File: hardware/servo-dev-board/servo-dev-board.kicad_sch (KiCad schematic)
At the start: 39 parts, among them J1 USB_B_Micro, J2 Conn_01x05_MountingPin, J3 Conn_01x04_MountingPin, J4 Conn_01x04_MountingPin, J5 Conn_02x05_Odd_Even, SW1 SW_Push, SW2 SW_Push, U1 DRV8231ADSGR, U2 SSP7615-33DFR, U3 STM32F301K8Ux, Y1 16MHz 9pF

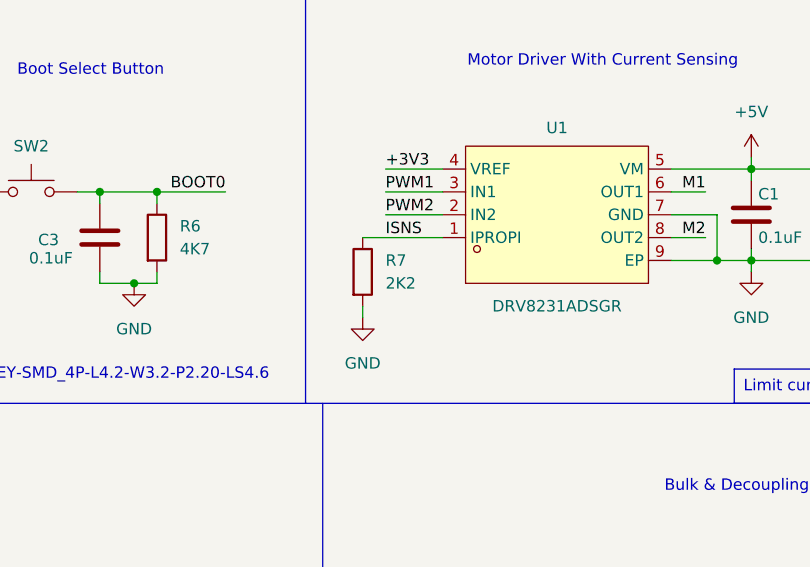
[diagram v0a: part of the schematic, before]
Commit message: Fixed error in PCB. Lowered isense resistor to 1.5k Ohm to increase max servo current to 1.5A
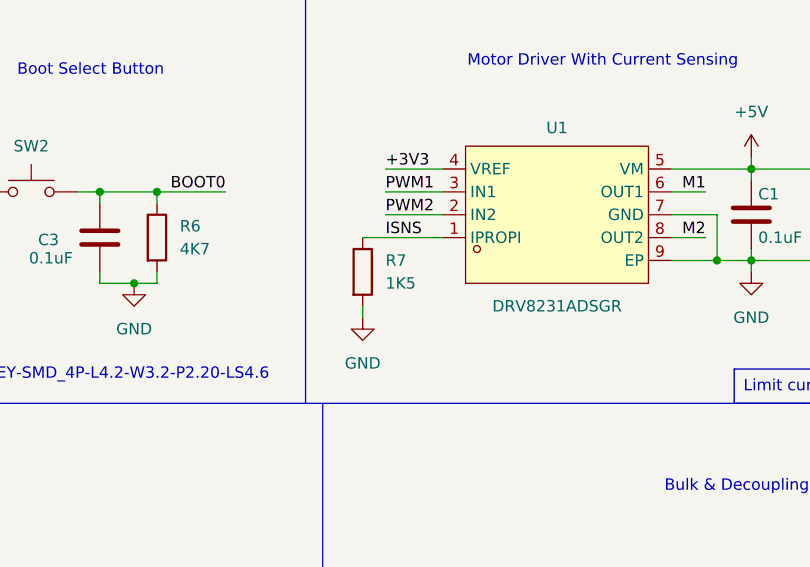
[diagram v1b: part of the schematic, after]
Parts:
- R7: value 2K2 -> 1K5; LCSC C25768 -> C25867
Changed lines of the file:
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@@
 			)
 		)
-		(property "Value" "2K2"
+		(property "Value" "1K5"
 			(at 110.49 88.8999 0)
 			(effects
@@
 			)
 		)
-		(property "LCSC" "C25768"
+		(property "LCSC" "C25867"
 			(at 110.49 86.3599 0)
 			(effects

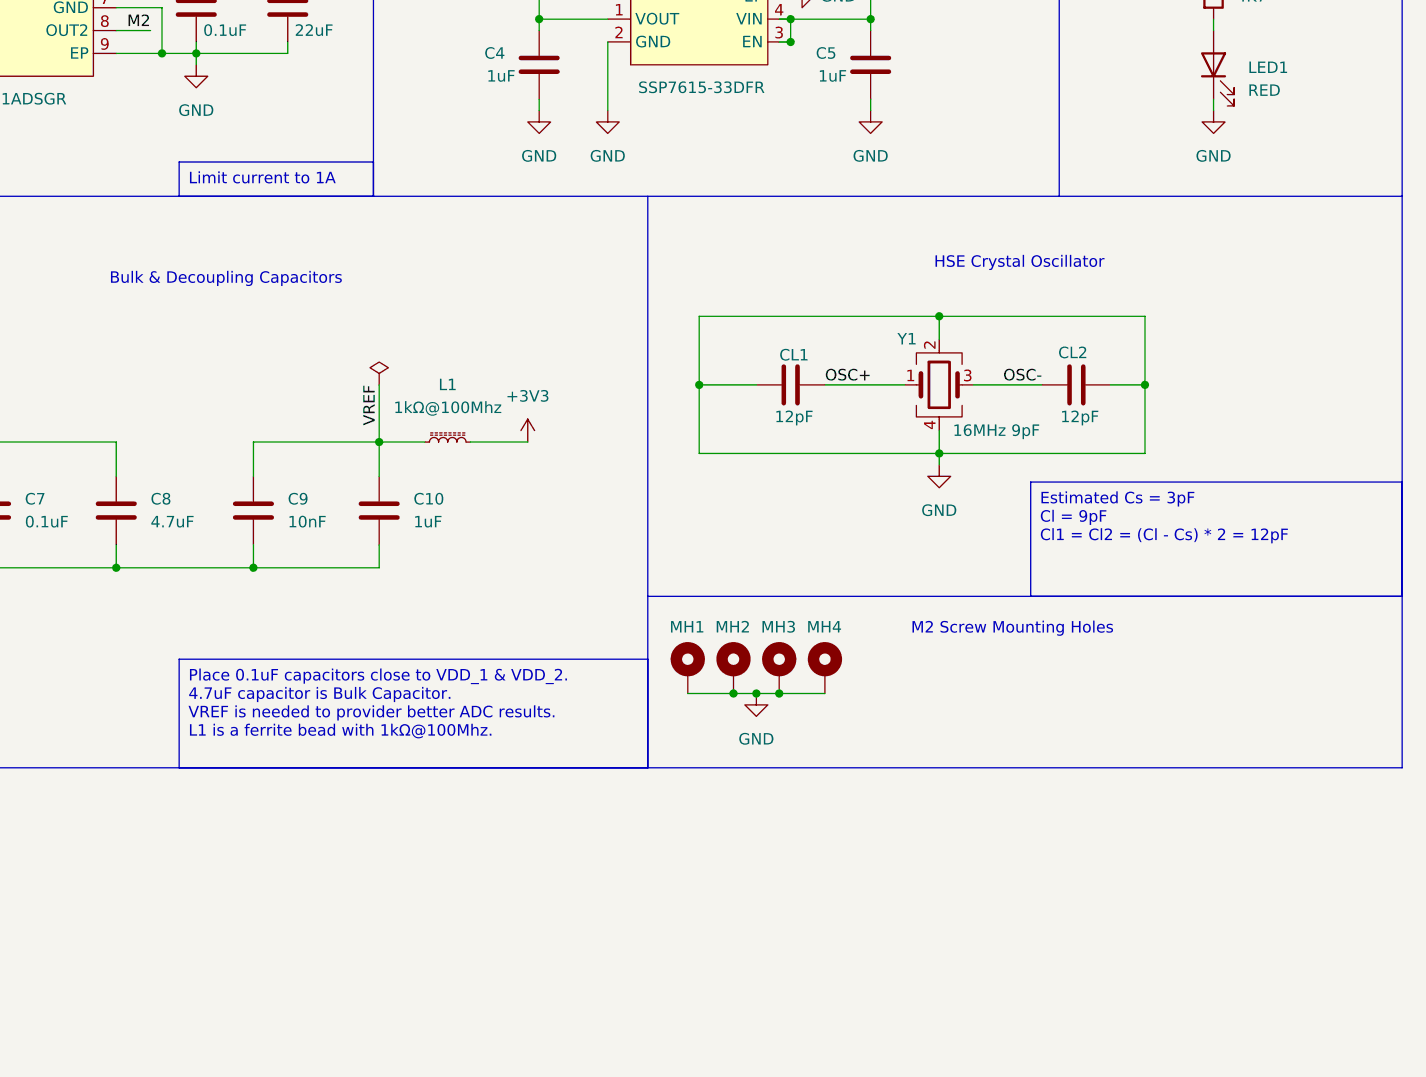
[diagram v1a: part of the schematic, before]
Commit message: added version, board, author info
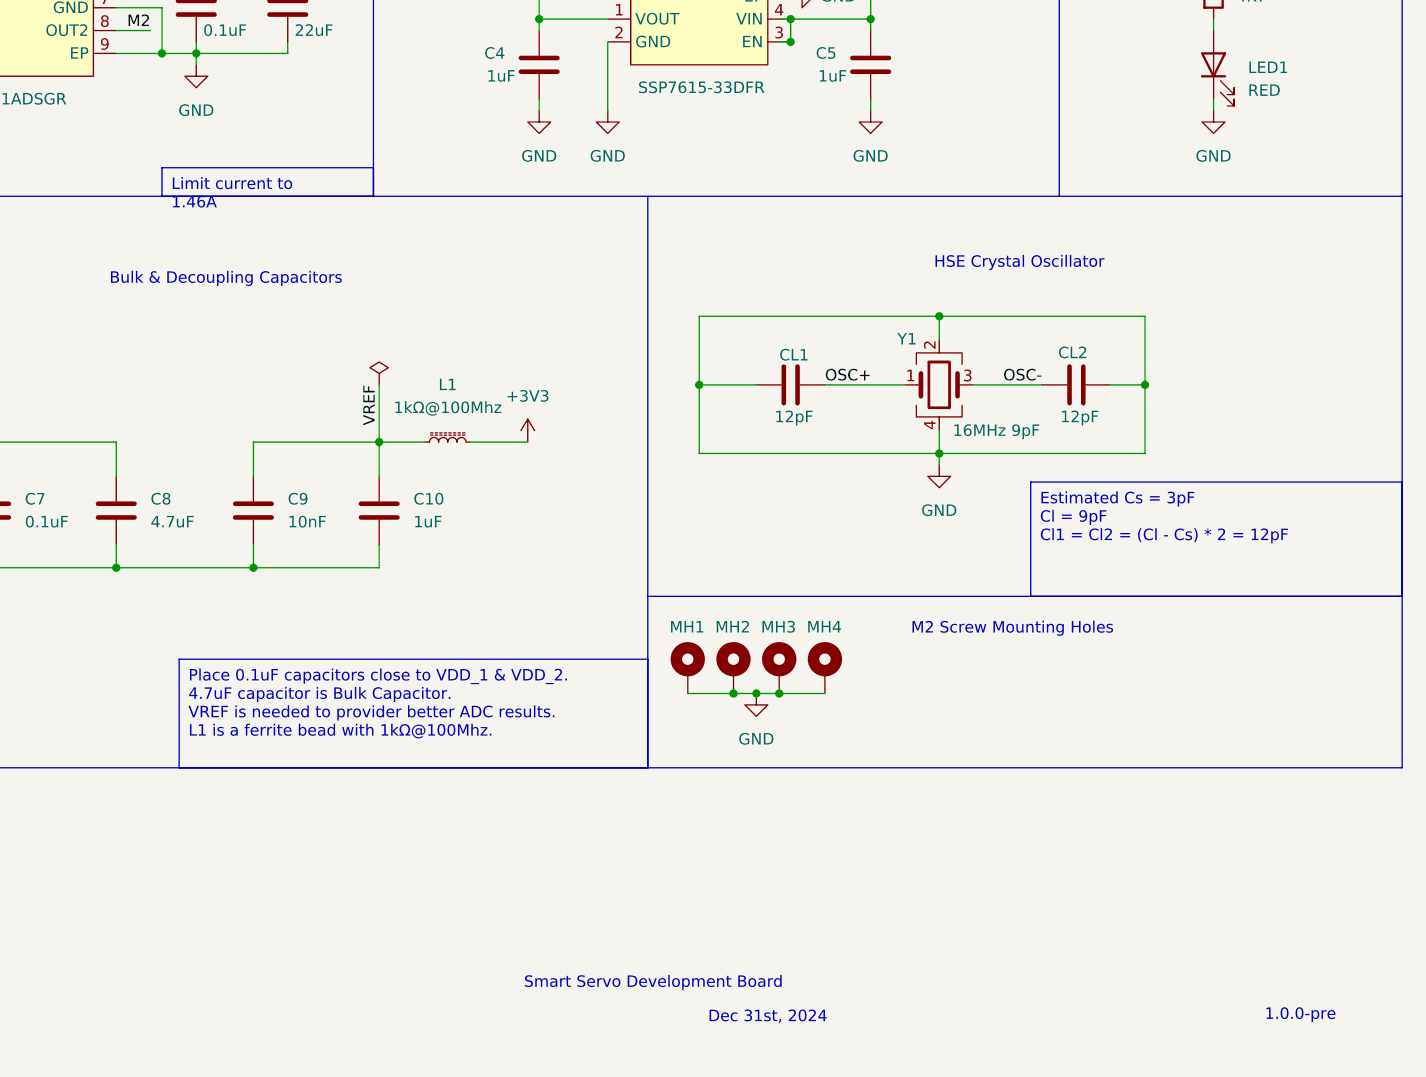
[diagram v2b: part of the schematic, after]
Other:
- note added: "1.0.0-pre"
- note added: "Dec 31st, 2024"
- note added: "Smart Servo Development Board"
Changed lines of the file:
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@@
 		)
 	)
-	(text_box "Limit current to 1A"
+	(text_box "Limit current to 1.46A"
 		(exclude_from_sim no)
-		(at 149.225 98.425 0)
-		(size 21.59 3.81)
+		(at 147.32 99.06 0)
+		(size 23.495 3.175)
 		(stroke
 			(width 0)
@@
 		)
 	)
+	(text "Dec 31st, 2024"
+		(exclude_from_sim no)
+		(at 214.63 193.548 0)
+		(effects
+			(font
+				(size 1.27 1.27)
+			)
+		)
+	)
 	(text "Reset Button"
 		(exclude_from_sim no)
 		(at 31.496 65.024 0)
+		(effects
+			(font
+				(size 1.27 1.27)
+			)
+		)
+	)
+	(text "Smart Servo Development Board"
+		(exclude_from_sim no)
+		(at 201.93 189.738 0)
 		(effects
 			(font
@@
 		(effects
 			(font
+				(size 1.27 1.27)
+			)
+		)
+	)
+	(text "1.0.0-pre"
+		(exclude_from_sim no)
+		(at 273.812 193.294 0)
+		(effects
+			(font

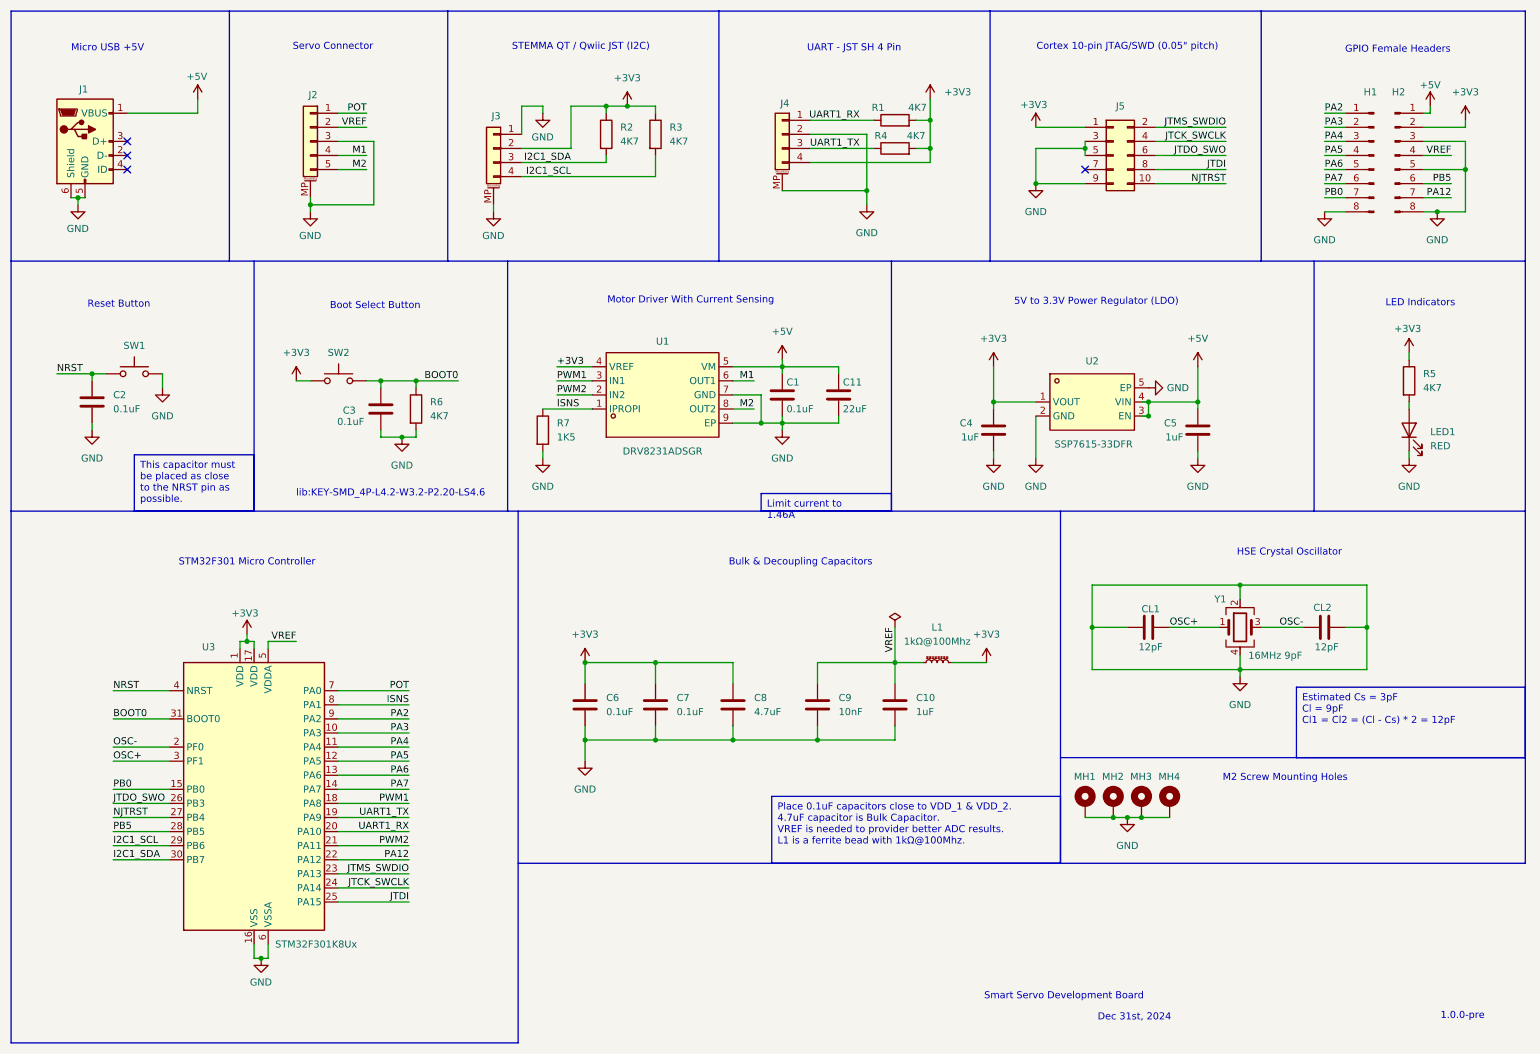
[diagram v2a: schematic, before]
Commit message: overhaul servo dev board to use ch32v00X
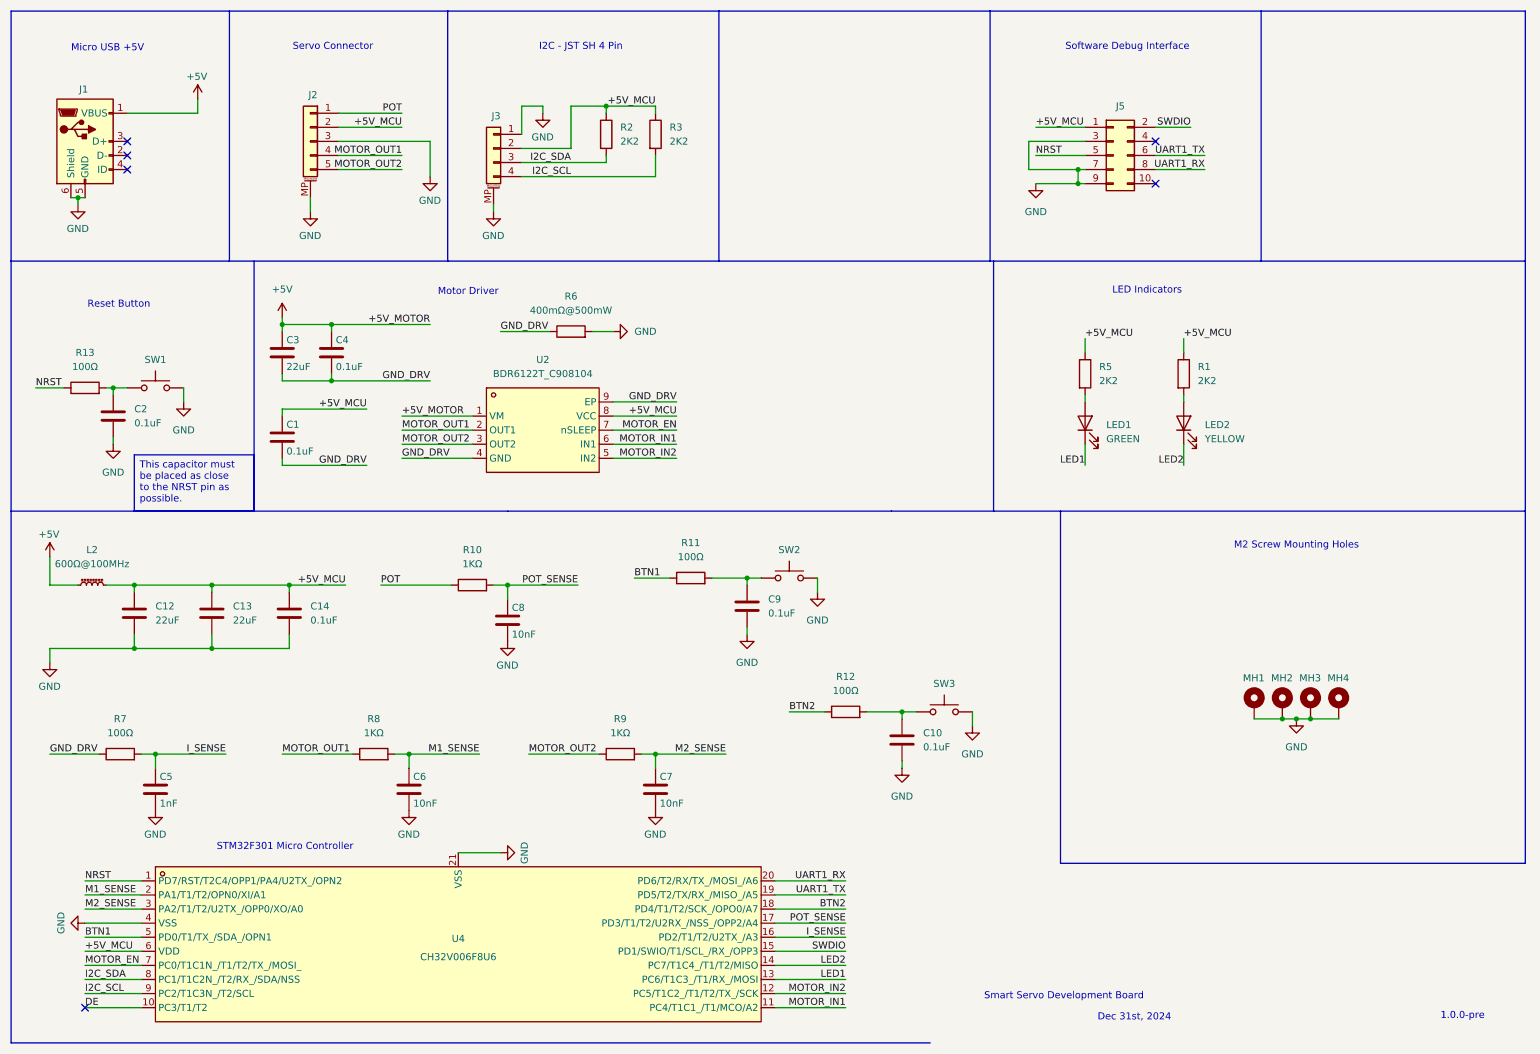
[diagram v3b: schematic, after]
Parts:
- removed C11: 22uF, Capacitor_SMD:C_0603_1608Metric, symbol Device:C
- removed CL1, CL2: 12pF, Capacitor_SMD:C_0402_1005Metric, symbol Device:C
- removed H1, H2: Conn_01x08_Pin, Connector_PinHeader_2.54mm:PinHeader_1x08_P2.54mm_Vertical, symbol Connector:Conn_01x08_Pin
- removed J4: Conn_01x04_MountingPin, Connector_JST:JST_SH_BM04B-SRSS-TB_1x04-1MP_P1.00mm_Vertical, symbol Connector_Generic_MountingPin:Conn_01x04_MountingPin
- removed L1: 1kΩ@100Mhz, Inductor_SMD:L_0402_1005Metric, symbol Device:L_Ferrite_Small
- removed R4: 4K7, Resistor_SMD:R_0402_1005Metric, symbol Device:R
- removed U1: DRV8231ADSGR, Package_SON:WSON-8-1EP_2x2mm_P0.5mm_EP0.9x1.6mm, symbol lib:DRV8231ADSGR
- removed U2: SSP7615-33DFR, Package_DFN_QFN:UDFN-4-1EP_1x1mm_P0.65mm_EP0.48x0.48mm, symbol lib:SSP7615-33DFR
- removed U3: STM32F301K8Ux, Package_DFN_QFN:QFN-32-1EP_5x5mm_P0.5mm_EP3.45x3.45mm, symbol MCU_ST_STM32F3:STM32F301K8Ux
- removed Y1: 16MHz 9pF, Crystal:Crystal_SMD_3225-4Pin_3.2x2.5mm, symbol Device:Crystal_GND24
- added C12: 22uF, Capacitor_SMD:C_1206_3216Metric, symbol Device:C
- added C13: 22uF, Capacitor_SMD:C_0402_1005Metric, symbol Device:C
- added C14: 0.1uF, Capacitor_SMD:C_0402_1005Metric, symbol Device:C
- added L2: 600Ω@100MHz, Inductor_SMD:L_0603_1608Metric, symbol Device:L_Ferrite_Small
- added LED2: YELLOW, LED_SMD:LED_0805_2012Metric, symbol Device:LED
- added R10, R8, R9: 1KΩ, Resistor_SMD:R_0402_1005Metric, symbol Device:R
- added R11: 100Ω, symbol Device:R
- added R12, R13: 100Ω, Resistor_SMD:R_0402_1005Metric, symbol Device:R
- added SW3: SW_Push, lib:SW-SMD_L3.9-W3.0-P4.45, symbol Switch:SW_Push
- added U2: BDR6122T_C908104, Package_DFN_QFN:WDFN-8-1EP_2x2mm_P0.5mm_EP0.8x1.2mm, symbol lib:BDR6122T_C908104
- added U4: CH32V006F8U6, Package_DFN_QFN:UQFN-20-1EP_3x3mm_P0.4mm_EP1.7x1.7mm, symbol lib:CH32V006F8U6
- C10, C4: value 1uF -> 0.1uF; LCSC C52923 -> C1525
- C3: value 0.1uF -> 22uF; LCSC C1525 -> (none)
- C5: value 1uF -> 1nF; LCSC C52923 -> C1523
- C6, C7: value 0.1uF -> 10nF; LCSC C1525 -> C15195
- C8: value 4.7uF -> 10nF; footprint Capacitor_SMD:C_0603_1608Metric -> Capacitor_SMD:C_0402_1005Metric; LCSC C19666 -> C15195
- C9: value 10nF -> 0.1uF; LCSC C15195 -> C1525
- LED1: value RED -> GREEN; footprint LED_SMD:LED_0603_1608Metric -> LED_SMD:LED_0805_2012Metric
- R1, R2, R3, R5: value 4K7 -> 2K2; LCSC C25792 -> C25879
- R6: value 4K7 -> 400mΩ@500mW; footprint Resistor_SMD:R_0402_1005Metric -> Resistor_SMD:R_1206_3216Metric; LCSC C25792 -> C912792
- R7: value 1K5 -> 100Ω; LCSC C25867 -> C25076
- SW1: footprint Button_Switch_SMD:SW_SPST_PTS810 -> lib:SW-SMD_L3.9-W3.0-P4.45; LCSC C221895 -> C720477
- SW2: LCSC C221895 -> C720477
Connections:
- net ISNS is gone; now on net GND_DRV: R7.1
- net JTDI is gone; now on net UART1_RX: J5.8 (Pin_8)
- net JTDO_SWO is gone; now on net UART1_TX: J5.6 (Pin_6)
- net +5V: now also C3.2, C4.2, L2.1, U2.1 (VM); no longer C1.2, C5.2
- net GND: now also J5.7 (Pin_7), MH1.MP, MH2.MP, MH3.MP, MH4.MP, SW2.2, C12.1, C13.1, C14.1, SW3.2, U4.21 (VSS), U4.4 (VSS); no longer C1.1, C3.2, C4.1, J5.5 (Pin_5), LED1.1 (K), MH1.1 (MP), MH2.1 (MP), MH3.1 (MP), MH4.1 (MP), R7.2
- net NRST: now also J5.5 (Pin_5), R13.1, U4.1 (PD7/RST/T2C4/OPP1/PA4/U2TX_/OPN2); no longer C2.2, SW1.1
- net POT: now also R10.1
- net UART1_RX: now also U4.20 (PD6/T2/RX/TX_/MOSI_/A6); no longer R1.1
- net UART1_TX: now also U4.19 (PD5/T2/TX/RX_/MISO_/A5)
- removed net +3V3: C4.2, C6.2, C7.2, C8.2, J3.2 (Pin_2), J5.1 (Pin_1), R1.2, R2.1, R3.1, R5.1, SW2.1
- net BOOT0 renamed GND_DRV
- net GND_DRV: now also C1.1, C4.1, U2.4 (GND), U2.9 (EP); no longer SW2.2
- net I2C1_SCL renamed I2C_SCL
- net I2C_SCL: now also U4.9 (PC2/T1C3N_/T2/SCL)
- net I2C1_SDA renamed I2C_SDA
- net I2C_SDA: now also U4.8 (PC1/T1C2N_/T2/RX_/SDA/NSS)
- net JTCK_SWCLK: no longer names the net of J5.4 (Pin_4)
- net JTMS_SWDIO renamed SWDIO
- net SWDIO: now also U4.15 (PD1/SWIO/T1/SCL_/RX_/OPP3)
- net M1 renamed MOTOR_OUT1
- net MOTOR_OUT1: now also R8.1, U2.2 (OUT1)
- net M2 renamed MOTOR_OUT2
- net MOTOR_OUT2: now also R9.1, U2.3 (OUT2)
- net NJTRST: no longer names the net of J5.10 (Pin_10)
- removed net VREF: C10.2, C9.2, J2.2 (Pin_2)
- new net: C9.2, R11.2, SW2.1
- new net: C10.2, R12.2, SW3.1
- new net: C2.2, R13.2, SW1.1
- new net: LED2.2 (A), R1.2
- new net +5V_MCU: C1.2, C12.2, C13.2, C14.2, J2.2 (Pin_2), J3.2 (Pin_2), J5.1 (Pin_1), L2.2, R1.1, R2.1, R3.1, R5.1, U2.8 (VCC), U4.6 (VDD)
- new net BTN1: R11.1, U4.5 (PD0/T1/TX_/SDA_/OPN1)
- new net BTN2: R12.1, U4.18 (PD4/T1/T2/SCK_/OPO0/A7)
- new net DE: U4.10 (PC3/T1/T2)
- new net I_SENSE: C5.2, R7.2, U4.16 (PD2/T1/T2/U2TX_/A3)
- new net LED1: LED1.1 (K), U4.13 (PC6/T1C3_/T1/RX_/MOSI)
- new net LED2: LED2.1 (K), U4.14 (PC7/T1C4_/T1/T2/MISO)
- new net M1_SENSE: C6.2, R8.2, U4.2 (PA1/T1/T2/OPN0/XI/A1)
- new net M2_SENSE: C7.2, R9.2, U4.3 (PA2/T1/T2/U2TX_/OPP0/XO/A0)
- new net MOTOR_EN: U2.7 (nSLEEP), U4.7 (PC0/T1C1N_/T1/T2/TX_/MOSI_)
- new net MOTOR_IN1: U2.6 (IN1), U4.11 (PC4/T1C1_/T1/MCO/A2)
- new net MOTOR_IN2: U2.5 (IN2), U4.12 (PC5/T1C2_/T1/T2/TX_/SCK)
- new net POT_SENSE: C8.2, R10.2, U4.17 (PD3/T1/T2/U2RX_/NSS_/OPP2/A4)
- no-connect marks 4 -> 6
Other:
- note added: "I2C - JST SH 4 Pin"
- note added: "Motor Driver"
- note added: "Software Debug Interface"
- note removed: "5V to 3.3V Power Regulator (LDO)"
- note removed: "Boot Select Button"
- note removed: "Bulk & Decoupling Capacitors"
- note removed: "Cortex 10-pin JTAG/SWD (0.05" pitch)"
- note removed: "GPIO Female Headers"
- note removed: "HSE Crystal Oscillator"
- note removed: "Motor Driver With Current Sensing"
- note removed: "STEMMA QT / Qwiic JST (I2C)"
- note removed: "UART - JST SH 4 Pin"
- note removed: "lib:KEY-SMD_4P-L4.2-W3.2-P2.20-LS4.6"
- moved on the sheet: C2, LED1, MH1, MH2, MH3, MH4, R5, SW1
